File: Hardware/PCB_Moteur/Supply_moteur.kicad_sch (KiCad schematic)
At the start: 27 parts, among them J1 XT30PW-F, U2 L6981N33DR

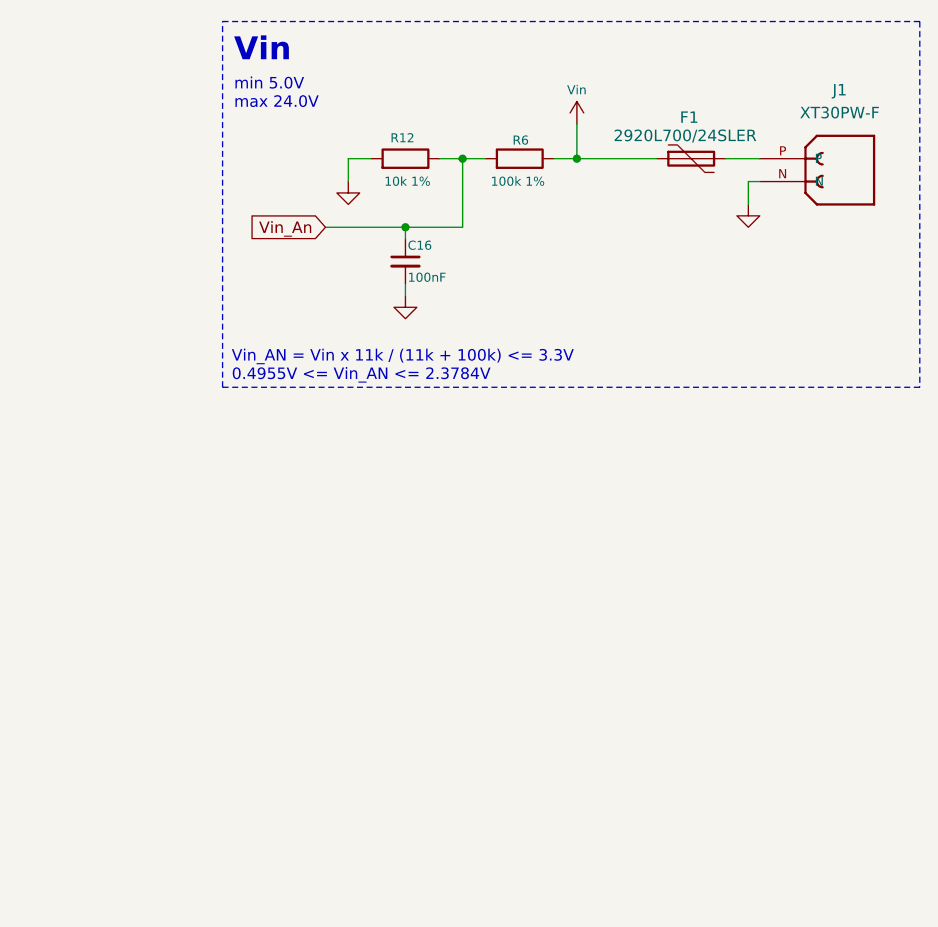
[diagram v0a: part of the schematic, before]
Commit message: fix(moteur + gse): gnd not connected for pressure sensor + seperate alim pressure sensor for motor pcb
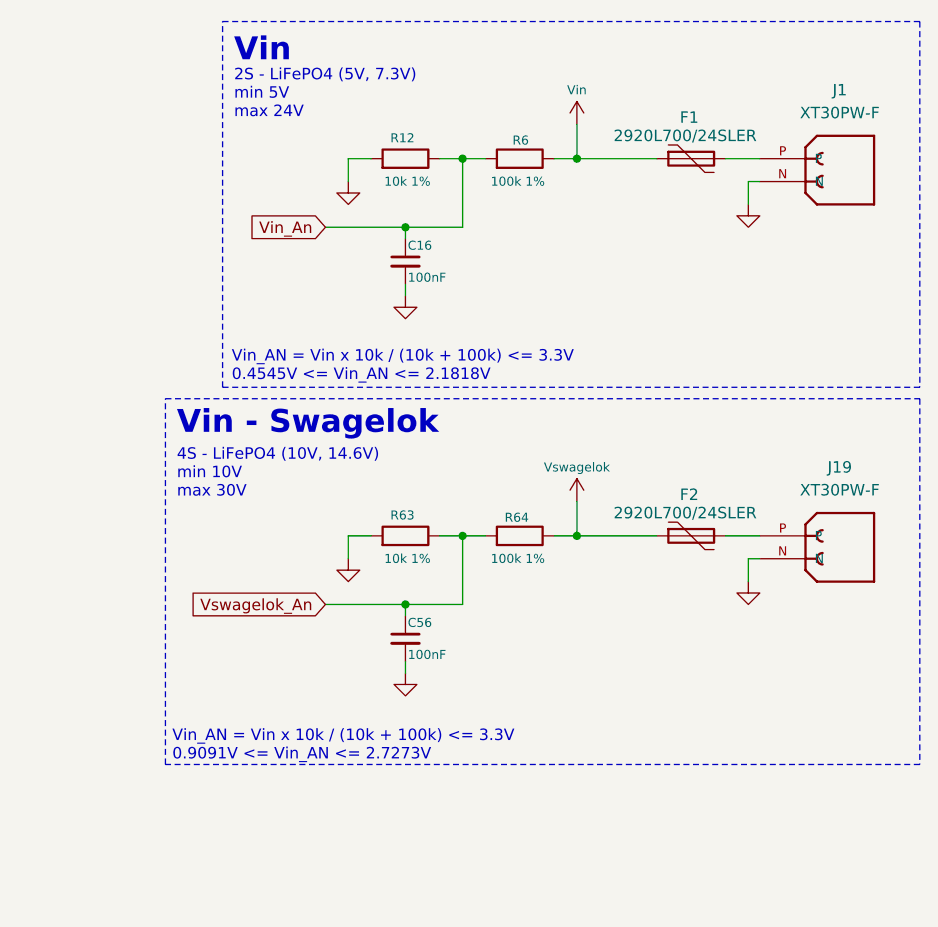
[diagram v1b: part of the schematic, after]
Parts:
- added C56: 100nF, Capacitor_SMD:C_0805_2012Metric, symbol Device:C_Small
- added F2: 2920L700/24SLER, Fuse:Fuse_2920_7451Metric, symbol Device:Polyfuse
- added J19: XT30PW-F, pcb_moteur:XT30PW-F, symbol pcb_moteur:XT30PW-F
- added R63: 10k 1%, Resistor_SMD:R_0805_2012Metric, symbol Device:R
- added R64: 100k 1%, Resistor_SMD:R_0805_2012Metric, symbol Device:R
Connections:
- net GND: now also C56.2, J19.N, R63.2
- new net: F2.2, J19.P
- new net Vswagelok: F2.1, R64.1
- new net Vswagelok_An: C56.1, R63.1, R64.2
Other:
- note added: "2S - LiFePO4 (5V, 7.3V) min 5V max 24V"
- note added: "4S - LiFePO4 (10V, 14.6V) min 10V max 30V"
- note added: "Vin - Swagelok"
- note added: "Vin_AN = Vin x 10k / (10k + 100k) <= 3.3V 0.4545V <= Vin_AN <= 2.1818V"
- note added: "Vin_AN = Vin x 10k / (10k + 100k) <= 3.3V 0.9091V <= Vin_AN <= 2.7273V"
- note removed: "Vin_AN = Vin x 11k / (11k + 100k) <= 3.3V 0.4955V <= Vin_AN <= 2.3784V"
- note removed: "min 5.0V max 24.0V"

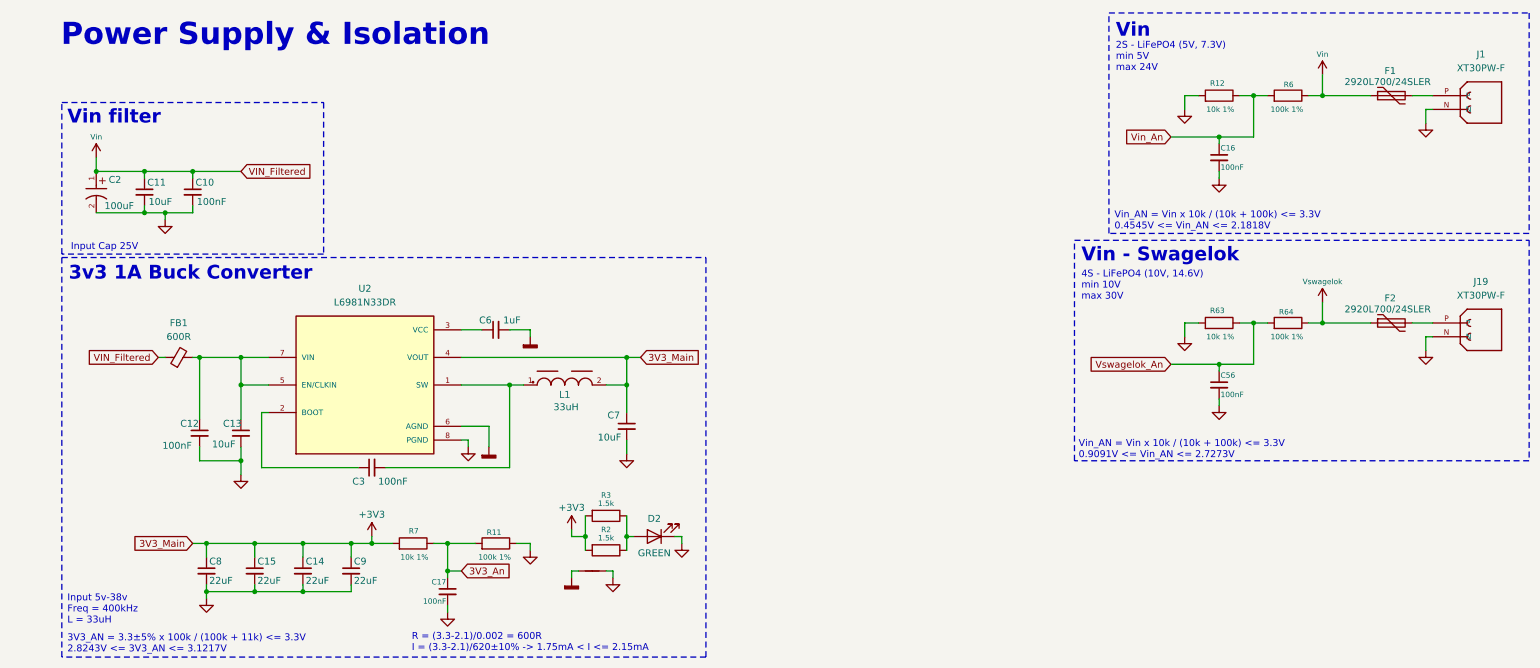
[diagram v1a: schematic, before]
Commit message: wip: new alim, power plane and pin changes
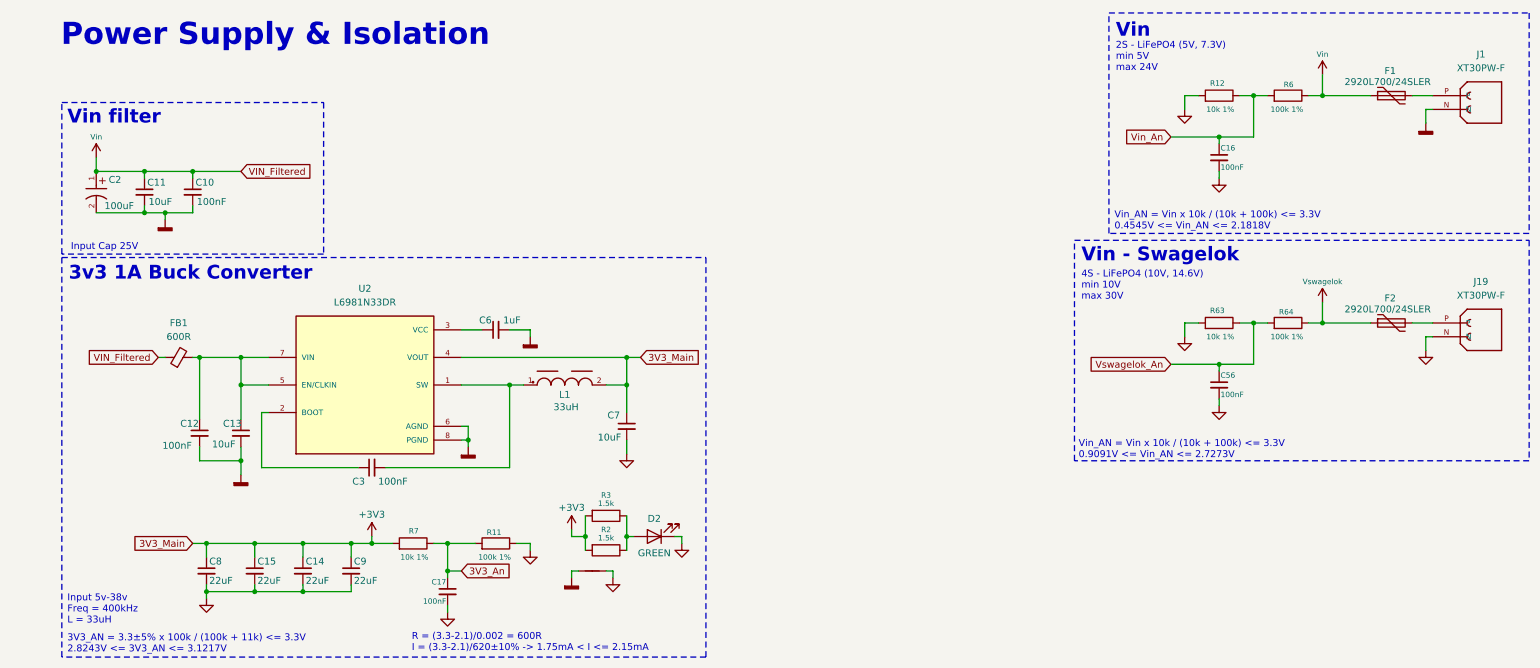
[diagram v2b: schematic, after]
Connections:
- net AGND3V3: now also C10.2, C11.2, C12.2, C13.2, C2.2, J1.N, U2.8 (PGND)
- net GND: no longer C10.2, C11.2, C12.2, C13.2, C2.2, J1.N, U2.8 (PGND)
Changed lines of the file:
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@@
 	)
 	(junction
+		(at 88.9 91.44)
+		(diameter 0)
+		(color 0 0 0 0)
+	)
+	(junction
 		(at 40.64 110.49)
 		(diameter 0)
@@
 	(wire
 		(pts
-			(xy 92.71 88.9) (xy 92.71 92.71)
+			(xy 88.9 88.9) (xy 88.9 91.44)
 		)
 		(stroke
@@
 	(wire
 		(pts
-			(xy 87.63 88.9) (xy 92.71 88.9)
+			(xy 87.63 88.9) (xy 88.9 88.9)
 		)
 		(stroke
@@
 	)
 	(symbol
+		(lib_id "power:GNDD")
+		(at 265.43 33.02 0)
+		(unit 1)
+		(exclude_from_sim no)
+		(in_bom yes)
+		(on_board yes)
+		(dnp no)
+		(fields_autoplaced yes)
+		(property "Reference" "#PWR078"
+			(at 265.43 39.37 0)
+			(effects
+				(font
+					(size 1.27 1.27)
+				)
+				(hide yes)
+			)
+		)
+		(property "Value" "AGND3V3"
+			(at 265.43 36.83 0)
+			(effects
+				(font
+					(size 1.27 1.27)
+				)
+				(hide yes)
+			)
+		)
+		(property "Footprint" ""
+			(at 265.43 33.02 0)
+			(effects
+				(font
+					(size 1.27 1.27)
+				)
+				(hide yes)
+			)
+		)
+		(property "Datasheet" ""
+			(at 265.43 33.02 0)
+			(effects
+				(font
+					(size 1.27 1.27)
+				)
+				(hide yes)
+			)
+		)
+		(property "Description" "Power symbol creates a global label with name \"GNDD\" , digital ground"
+			(at 265.43 33.02 0)
+			(effects
+				(font
+					(size 1.27 1.27)
+				)
+				(hide yes)
+			)
+		)
+		(pin "1"
+		)
+		(instances
+			(project "PCB_moteur"
+				(path "/b0d87684-7b1c-41d8-8358-755aa327573e/92d1df5d-a307-4eea-a65c-ade4cb0ad548"
+					(reference "#PWR078")
+					(unit 1)
+				)
+			)
+		)
+	)
+	(symbol
 		(lib_id "power:GND")
 		(at 115.57 116.84 0)
@@
 	(symbol
 		(lib_id "power:GNDD")
-		(at 92.71 92.71 0)
+		(at 88.9 92.71 0)
 		(unit 1)
 		(exclude_from_sim no)
@@
 		(fields_autoplaced yes)
 		(property "Reference" "#PWR0112"
-			(at 92.71 99.06 0)
+			(at 88.9 99.06 0)
 			(effects
 				(font
@@
 		)
 		(property "Value" "AGND3V3"
-			(at 92.71 96.52 0)
+			(at 88.9 96.52 0)
 			(effects
 				(font
@@
 		)
 		(property "Footprint" ""
-			(at 92.71 92.71 0)
+			(at 88.9 92.71 0)
 			(effects
 				(font
@@
 		)
 		(property "Datasheet" ""
-			(at 92.71 92.71 0)
+			(at 88.9 92.71 0)
 			(effects
 				(font
@@
 		)
 		(property "Description" "Power symbol creates a global label with name \"GNDD\" , digital ground"
-			(at 92.71 92.71 0)
+			(at 88.9 92.71 0)
 			(effects
 				(font
@@
 	)
 	(symbol
-		(lib_id "power:GND")
-		(at 265.43 33.02 0)
+		(lib_id "power:GNDD")
+		(at 46.99 97.79 0)
 		(unit 1)
 		(exclude_from_sim no)
@@
 		(dnp no)
 		(fields_autoplaced yes)
-		(property "Reference" "#PWR0101"
-			(at 265.43 39.37 0)
-			(effects
-				(font
-					(size 1 1)
-				)
-				(hide yes)
-			)
-		)
-		(property "Value" "GND"
-			(at 265.43 38.1 0)
-			(effects
-				(font
-					(size 1 1)
-				)
-				(hide yes)
-			)
-		)
-		(property "Footprint" ""
-			(at 265.43 33.02 0)
-			(effects
-				(font
-					(size 1 1)
-				)
-				(hide yes)
-			)
-		)
-		(property "Datasheet" ""
-			(at 265.43 33.02 0)
-			(effects
-				(font
-					(size 1 1)
-				)
-				(hide yes)
-			)
-		)
-		(property "Description" ""
-			(at 265.43 33.02 0)
+		(property "Reference" "#PWR075"
+			(at 46.99 104.14 0)
 			(effects
 				(font
@@
 			)
 		)
-		(pin "1"
-		)
-		(instances
-			(project "PCB_moteur"
-				(path "/b0d87684-7b1c-41d8-8358-755aa327573e/92d1df5d-a307-4eea-a65c-ade4cb0ad548"
-					(reference "#PWR0101")
-					(unit 1)
-				)
-			)
-		)
-	)
-	(symbol
-		(lib_id "power:GND")
-		(at 88.9 92.71 0)
-		(unit 1)
-		(exclude_from_sim no)
-		(in_bom yes)
-		(on_board yes)
-		(dnp no)
-		(fields_autoplaced yes)
-		(property "Reference" "#PWR0111"
-			(at 88.9 99.06 0)
-			(effects
-				(font
-					(size 1 1)
-				)
-				(hide yes)
-			)
-		)
-		(property "Value" "GND"
-			(at 88.9 97.79 0)
+		(property "Value" "AGND3V3"
+			(at 46.99 101.6 0)
 			(effects
 				(font
-					(size 1 1)
+					(size 1.27 1.27)
 				)
 				(hide yes)
@@
 		)
 		(property "Footprint" ""
-			(at 88.9 92.71 0)
+			(at 46.99 97.79 0)
 			(effects
 				(font
-					(size 1 1)
+					(size 1.27 1.27)
 				)
 				(hide yes)
@@
 		)
 		(property "Datasheet" ""
-			(at 88.9 92.71 0)
+			(at 46.99 97.79 0)
 			(effects
 				(font
-					(size 1 1)
+					(size 1.27 1.27)
 				)
 				(hide yes)
 			)
 		)
-		(property "Description" ""
-			(at 88.9 92.71 0)
+		(property "Description" "Power symbol creates a global label with name \"GNDD\" , digital ground"
+			(at 46.99 97.79 0)
 			(effects
 				(font
@@
 			(project "PCB_moteur"
 				(path "/b0d87684-7b1c-41d8-8358-755aa327573e/92d1df5d-a307-4eea-a65c-ade4cb0ad548"
-					(reference "#PWR0111")
+					(reference "#PWR075")
 					(unit 1)
 				)
@@
 	)
 	(symbol
-		(lib_id "power:GND")
-		(at 33.02 50.8 0)
-		(unit 1)
-		(exclude_from_sim no)
-		(in_bom yes)
-		(on_board yes)
-		(dnp no)
-		(fields_autoplaced yes)
-		(property "Reference" "#PWR034"
-			(at 33.02 57.15 0)
-			(effects
-				(font
-					(size 1 1)
-				)
-				(hide yes)
-			)
-		)
-		(property "Value" "GND"
-			(at 33.02 55.88 0)
-			(effects
-				(font
-					(size 1 1)
-				)
-				(hide yes)
-			)
-		)
-		(property "Footprint" ""
-			(at 33.02 50.8 0)
-			(effects
-				(font
-					(size 1 1)
-				)
-				(hide yes)
-			)
-		)
-		(property "Datasheet" ""
-			(at 33.02 50.8 0)
-			(effects
-				(font
-					(size 1 1)
-				)
-				(hide yes)
-			)
-		)
-		(property "Description" ""
-			(at 33.02 50.8 0)
-			(effects
-				(font
-					(size 1.27 1.27)
-				)
-				(hide yes)
-			)
-		)
-		(pin "1"
-		)
-		(instances
-			(project "PCB_moteur"
-				(path "/b0d87684-7b1c-41d8-8358-755aa327573e/92d1df5d-a307-4eea-a65c-ade4cb0ad548"
-					(reference "#PWR034")
-					(unit 1)
-				)
-			)
-		)
-	)
-	(symbol
 		(lib_id "Device:C_Small")
 		(at 40.64 115.57 0)
@@
 	)
 	(symbol
+		(lib_id "power:GNDD")
+		(at 33.02 50.8 0)
+		(unit 1)
+		(exclude_from_sim no)
+		(in_bom yes)
+		(on_board yes)
+		(dnp no)
+		(fields_autoplaced yes)
+		(property "Reference" "#PWR034"
+			(at 33.02 57.15 0)
+			(effects
+				(font
+					(size 1.27 1.27)
+				)
+				(hide yes)
+			)
+		)
+		(property "Value" "AGND3V3"
+			(at 33.02 54.61 0)
+			(effects
+				(font
+					(size 1.27 1.27)
+				)
+				(hide yes)
+			)
+		)
+		(property "Footprint" ""
+			(at 33.02 50.8 0)
+			(effects
+				(font
+					(size 1.27 1.27)
+				)
+				(hide yes)
+			)
+		)
+		(property "Datasheet" ""
+			(at 33.02 50.8 0)
+			(effects
+				(font
+					(size 1.27 1.27)
+				)
+				(hide yes)
+			)
+		)
+		(property "Description" "Power symbol creates a global label with name \"GNDD\" , digital ground"
+			(at 33.02 50.8 0)
+			(effects
+				(font
+					(size 1.27 1.27)
+				)
+				(hide yes)
+			)
+		)
+		(pin "1"
+		)
+		(instances
+			(project "PCB_moteur"
+				(path "/b0d87684-7b1c-41d8-8358-755aa327573e/92d1df5d-a307-4eea-a65c-ade4cb0ad548"
+					(reference "#PWR034")
+					(unit 1)
+				)
+			)
+		)
+	)
+	(symbol
 		(lib_id "Device:C_Small")
 		(at 58.42 115.57 0)
@@
 					(unit 1)
 				)
-			)
-		)
-	)
-	(symbol
-		(lib_id "power:GND")
-		(at 46.99 97.79 0)
-		(unit 1)
-		(exclude_from_sim no)
-		(in_bom yes)
-		(on_board yes)
-		(dnp no)
-		(fields_autoplaced yes)
-		(property "Reference" "#PWR096"
-			(at 46.99 104.14 0)
-			(effects
-				(font
-					(size 1 1)
-				)
-				(hide yes)
-			)
-		)
-		(property "Value" "GND"
-			(at 46.99 102.87 0)
-			(effects
-				(font
-					(size 1 1)
-				)
-				(hide yes)
-			)
-		)
-		(property "Footprint" ""
-			(at 46.99 97.79 0)
-			(effects
-				(font
-					(size 1 1)
-				)
-				(hide yes)
-			)
-		)
-		(property "Datasheet" ""
-			(at 46.99 97.79 0)
-			(effects
-				(font
-					(size 1 1)
-				)
-				(hide yes)
-			)
-		)
-		(property "Description" ""
-			(at 46.99 97.79 0)
-			(effects
-				(font
-					(size 1.27 1.27)
-				)
-				(hide yes)
-			)
-		)
-		(pin "1"
-		)
-		(instances
-			(project "PCB_moteur"
-				(path "/b0d87684-7b1c-41d8-8358-755aa327573e/92d1df5d-a307-4eea-a65c-ade4cb0ad548"
-					(reference "#PWR096")
-					(unit 1)
-				)

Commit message: fix(moteur + gse): move xt30 to border + fix silkscreen + connect shield to gnd  in pressure sensor + remake rounded corners + fix/add doc
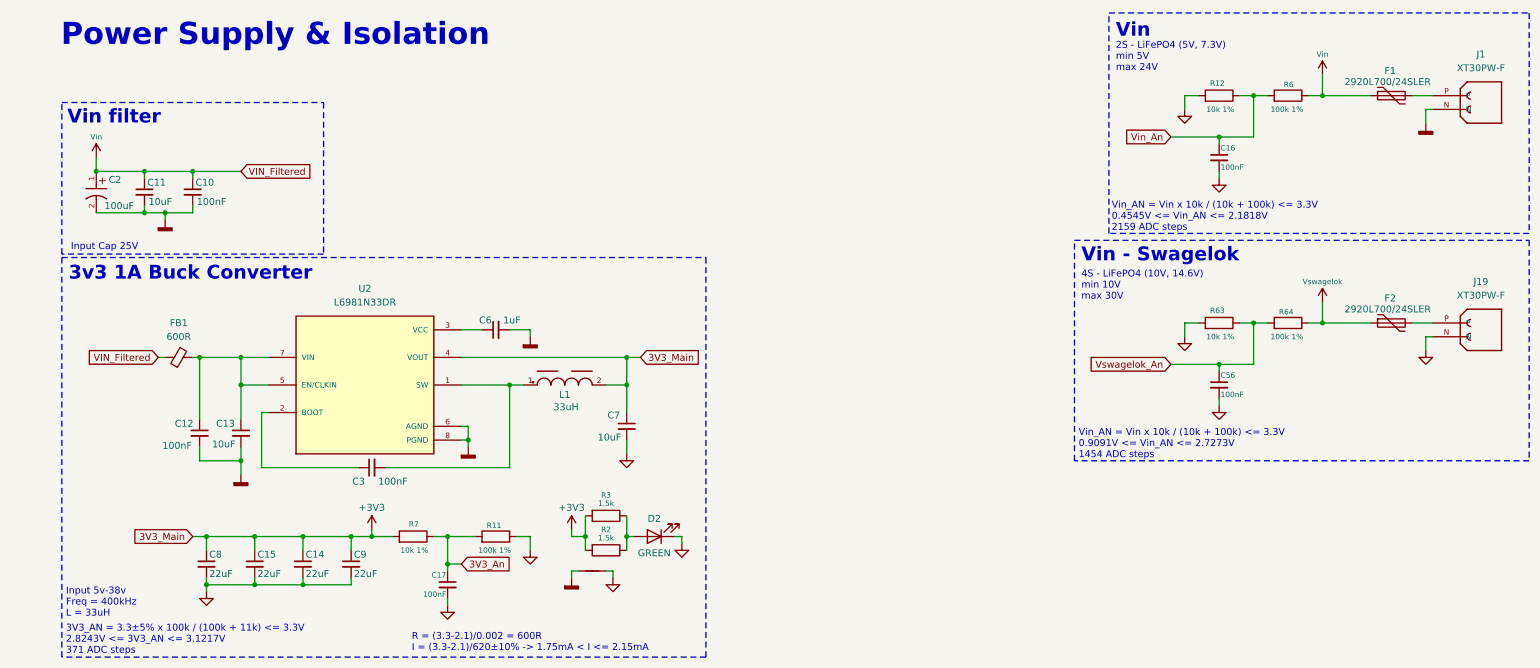
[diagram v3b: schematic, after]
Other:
- note added: "3V3_AN = 3.3±5% x 100k / (100k + 11k) <= 3.3V 2.8243V <= 3V3_AN <= 3.1217V 371 ADC steps"
- note added: "Vin_AN = Vin x 10k / (10k + 100k) <= 3.3V 0.4545V <= Vin_AN <= 2.1818V 2159 ADC steps"
- note added: "Vin_AN = Vin x 10k / (10k + 100k) <= 3.3V 0.9091V <= Vin_AN <= 2.7273V 1454 ADC steps"
- note removed: "3V3_AN = 3.3±5% x 100k / (100k + 11k) <= 3.3V 2.8243V <= 3V3_AN <= 3.1217V"
- note removed: "Vin_AN = Vin x 10k / (10k + 100k) <= 3.3V 0.4545V <= Vin_AN <= 2.1818V"
- note removed: "Vin_AN = Vin x 10k / (10k + 100k) <= 3.3V 0.9091V <= Vin_AN <= 2.7273V"
- moved on the sheet: C14, C15, C17, C8, C9, R11, R7
